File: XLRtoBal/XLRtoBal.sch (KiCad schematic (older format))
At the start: 60 parts, among them J1 XLR4BODYPIN, J10 SMAPCB, J11 SMAPCB, J12 Conn_01x02, J2 Conn_01x04, J3 Conn_01x04, J4 XLR4BODYPIN, J5 Conn_01x04, J6 Conn_01x01, J7 Conn_01x01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

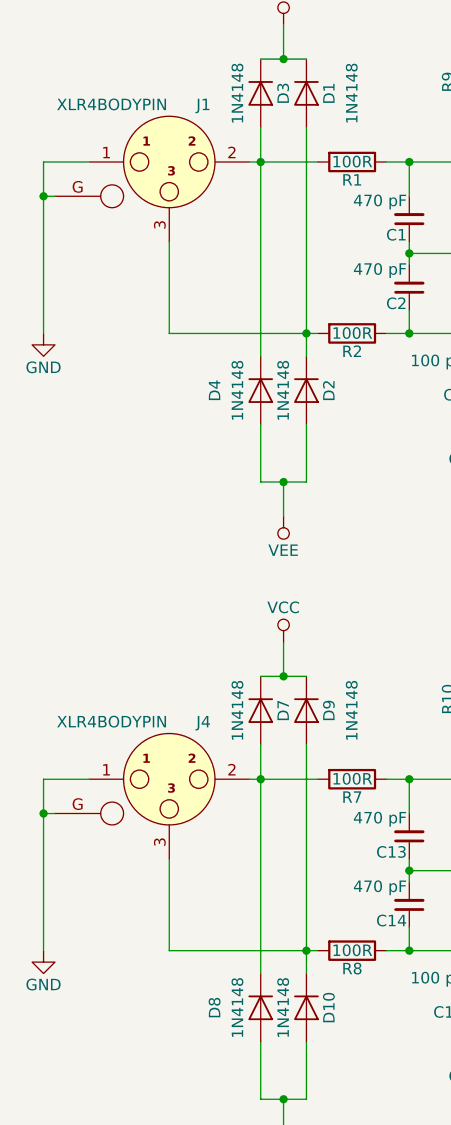
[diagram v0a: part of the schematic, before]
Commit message: Fixed some silkscreening
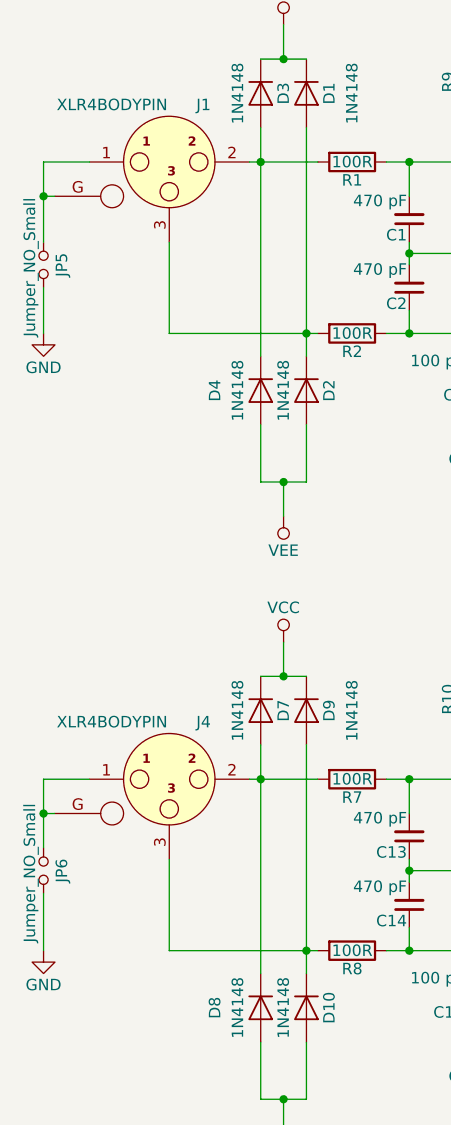
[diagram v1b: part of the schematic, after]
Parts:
- added JP5, JP6: Jumper_NO_Small, Pin_Headers:Pin_Header_Straight_1x02_Pitch2.54mm, symbol Jumper_NO_Small
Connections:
- net GND: now also JP5.2, JP6.2; no longer J1.1, J1.G, J4.1, J4.G
- new net: J1.1, J1.G, JP5.1
- new net: J4.1, J4.G, JP6.1
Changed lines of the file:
@@
 $EndDescr
 $Comp
-L GND #PWR01
+L GND #PWR1
 U 1 1 5F3D3B65
 P 1800 2600
-F 0 "#PWR01" H 1800 2350 50  0001 C CNN
+F 0 "#PWR1" H 1800 2350 50  0001 C CNN
 F 1 "GND" H 1800 2450 50  0000 C CNN
 F 2 "" H 1800 2600 50  0001 C CNN
@@
 $EndComp
 $Comp
-L GND #PWR02
+L GND #PWR7
 U 1 1 5F3D3E2D
 P 3650 3000
-F 0 "#PWR02" H 3650 2750 50  0001 C CNN
+F 0 "#PWR7" H 3650 2750 50  0001 C CNN
 F 1 "GND" H 3650 2850 50  0000 C CNN
 F 2 "" H 3650 3000 50  0001 C CNN
@@
 $EndComp
 $Comp
-L VEE #PWR03
+L VEE #PWR11
 U 1 1 5F3D40DD
 P 4050 2700
-F 0 "#PWR03" H 4050 2550 50  0001 C CNN
+F 0 "#PWR11" H 4050 2550 50  0001 C CNN
 F 1 "VEE" H 4050 2850 50  0000 C CNN
 F 2 "" H 4050 2700 50  0001 C CNN
@@
 $EndComp
 $Comp
-L VCC #PWR04
+L VCC #PWR15
 U 1 1 5F3D4122
 P 5300 1450
-F 0 "#PWR04" H 5300 1300 50  0001 C CNN
+F 0 "#PWR15" H 5300 1300 50  0001 C CNN
 F 1 "VCC" H 5300 1600 50  0000 C CNN
 F 2 "" H 5300 1450 50  0001 C CNN
@@
 $EndComp
 $Comp
-L GND #PWR05
+L GND #PWR13
 U 1 1 5F3D428D
 P 4250 3000
-F 0 "#PWR05" H 4250 2750 50  0001 C CNN
+F 0 "#PWR13" H 4250 2750 50  0001 C CNN
 F 1 "GND" H 4250 2850 50  0000 C CNN
 F 2 "" H 4250 3000 50  0001 C CNN
@@
 $EndComp
 $Comp
-L GND #PWR06
+L GND #PWR17
 U 1 1 5F3D4412
 P 5450 1750
-F 0 "#PWR06" H 5450 1500 50  0001 C CNN
+F 0 "#PWR17" H 5450 1500 50  0001 C CNN
 F 1 "GND" H 5450 1600 50  0000 C CNN
 F 2 "" H 5450 1750 50  0001 C CNN
@@
 $EndComp
 $Comp
-L GND #PWR07
+L GND #PWR9
 U 1 1 5F3D44EC
 P 3950 1950
-F 0 "#PWR07" H 3950 1700 50  0001 C CNN
+F 0 "#PWR9" H 3950 1700 50  0001 C CNN
 F 1 "GND" H 3950 1800 50  0000 C CNN
 F 2 "" H 3950 1950 50  0001 C CNN
@@
 $EndComp
 $Comp
-L VCC #PWR08
+L VCC #PWR3
 U 1 1 5F3D4787
 P 2850 1250
-F 0 "#PWR08" H 2850 1100 50  0001 C CNN
+F 0 "#PWR3" H 2850 1100 50  0001 C CNN
 F 1 "VCC" H 2850 1400 50  0000 C CNN
 F 2 "" H 2850 1250 50  0001 C CNN
@@
 $EndComp
 $Comp
-L VEE #PWR09
+L VEE #PWR4
 U 1 1 5F3D4918
 P 2850 3400
-F 0 "#PWR09" H 2850 3250 50  0001 C CNN
+F 0 "#PWR4" H 2850 3250 50  0001 C CNN
 F 1 "VEE" H 2850 3550 50  0000 C CNN
 F 2 "" H 2850 3400 50  0001 C CNN
@@
 $EndComp
 $Comp
-L GND #PWR010
+L GND #PWR19
 U 1 1 5F3D4B80
 P 6000 2500
-F 0 "#PWR010" H 6000 2250 50  0001 C CNN
+F 0 "#PWR19" H 6000 2250 50  0001 C CNN
 F 1 "GND" H 6000 2350 50  0000 C CNN
 F 2 "" H 6000 2500 50  0001 C CNN
@@
 $EndComp
 $Comp
-L GND #PWR011
+L GND #PWR28
 U 1 1 5F3D5397
 P 8950 2600
-F 0 "#PWR011" H 8950 2350 50  0001 C CNN
+F 0 "#PWR28" H 8950 2350 50  0001 C CNN
 F 1 "GND" H 8950 2450 50  0000 C CNN
 F 2 "" H 8950 2600 50  0001 C CNN
@@
 $EndComp
 $Comp
-L VCC #PWR012
+L VCC #PWR32
 U 1 1 5F3D57A3
 P 10000 1950
-F 0 "#PWR012" H 10000 1800 50  0001 C CNN
+F 0 "#PWR32" H 10000 1800 50  0001 C CNN
 F 1 "VCC" H 10000 2100 50  0000 C CNN
 F 2 "" H 10000 1950 50  0001 C CNN
@@
 $EndComp
 $Comp
-L GND #PWR013
+L GND #PWR25
 U 1 1 5F3D5C25
 P 8500 1250
-F 0 "#PWR013" H 8500 1000 50  0001 C CNN
+F 0 "#PWR25" H 8500 1000 50  0001 C CNN
 F 1 "GND" H 8500 1100 50  0000 C CNN
 F 2 "" H 8500 1250 50  0001 C CNN
@@
 $EndComp
 $Comp
-L GND #PWR014
+L GND #PWR33
 U 1 1 5F3D5DB2
 P 10000 2900
-F 0 "#PWR014" H 10000 2650 50  0001 C CNN
+F 0 "#PWR33" H 10000 2650 50  0001 C CNN
 F 1 "GND" H 10000 2750 50  0000 C CNN
 F 2 "" H 10000 2900 50  0001 C CNN
@@
 $EndComp
 $Comp
-L VEE #PWR015
+L VEE #PWR30
 U 1 1 5F3D67F6
 P 9500 3200
-F 0 "#PWR015" H 9500 3050 50  0001 C CNN
+F 0 "#PWR30" H 9500 3050 50  0001 C CNN
 F 1 "VEE" H 9500 3350 50  0000 C CNN
 F 2 "" H 9500 3200 50  0001 C CNN
@@
 $EndComp
 $Comp
-L GND #PWR016
+L GND #PWR35
 U 1 1 5F3D82E9
 P 10500 2900
-F 0 "#PWR016" H 10500 2650 50  0001 C CNN
+F 0 "#PWR35" H 10500 2650 50  0001 C CNN
 F 1 "GND" H 10500 2750 50  0000 C CNN
 F 2 "" H 10500 2900 50  0001 C CNN
@@
 $EndComp
 $Comp
-L GND #PWR017
+L GND #PWR27
 U 1 1 5F3D8979
 P 8750 2300
-F 0 "#PWR017" H 8750 2050 50  0001 C CNN
+F 0 "#PWR27" H 8750 2050 50  0001 C CNN
 F 1 "GND" H 8750 2150 50  0000 C CNN
 F 2 "" H 8750 2300 50  0001 C CNN
@@
 $EndComp
 $Comp
-L GND #PWR018
+L GND #PWR24
 U 1 1 5F3D8B1C
 P 8400 2650
-F 0 "#PWR018" H 8400 2400 50  0001 C CNN
+F 0 "#PWR24" H 8400 2400 50  0001 C CNN
 F 1 "GND" H 8400 2500 50  0000 C CNN
 F 2 "" H 8400 2650 50  0001 C CNN
@@
 $EndComp
 $Comp
-L GND #PWR019
+L GND #PWR29
 U 1 1 5F3DA1A1
 P 9500 1200
-F 0 "#PWR019" H 9500 950 50  0001 C CNN
+F 0 "#PWR29" H 9500 950 50  0001 C CNN
 F 1 "GND" H 9500 1050 50  0000 C CNN
 F 2 "" H 9500 1200 50  0001 C CNN
@@
 $EndComp
 $Comp
-L GND #PWR020
+L GND #PWR31
 U 1 1 5F3DA52E
 P 9700 3600
-F 0 "#PWR020" H 9700 3350 50  0001 C CNN
+F 0 "#PWR31" H 9700 3350 50  0001 C CNN
 F 1 "GND" H 9700 3450 50  0000 C CNN
 F 2 "" H 9700 3600 50  0001 C CNN
@@
 $EndComp
 $Comp
-L GND #PWR021
+L GND #PWR2
 U 1 1 5F3DAB4A
 P 1800 5300
-F 0 "#PWR021" H 1800 5050 50  0001 C CNN
+F 0 "#PWR2" H 1800 5050 50  0001 C CNN
 F 1 "GND" H 1800 5150 50  0000 C CNN
 F 2 "" H 1800 5300 50  0001 C CNN
@@
 $EndComp
 $Comp
-L GND #PWR022
+L GND #PWR8
 U 1 1 5F3DAB6E
 P 3650 5700
-F 0 "#PWR022" H 3650 5450 50  0001 C CNN
+F 0 "#PWR8" H 3650 5450 50  0001 C CNN
 F 1 "GND" H 3650 5550 50  0000 C CNN
 F 2 "" H 3650 5700 50  0001 C CNN
@@
 $EndComp
 $Comp
-L VEE #PWR023
+L VEE #PWR12
 U 1 1 5F3DAB7A
 P 4050 5400
-F 0 "#PWR023" H 4050 5250 50  0001 C CNN
+F 0 "#PWR12" H 4050 5250 50  0001 C CNN
 F 1 "VEE" H 4050 5550 50  0000 C CNN
 F 2 "" H 4050 5400 50  0001 C CNN
@@
 $EndComp
 $Comp
-L VCC #PWR024
+L VCC #PWR16
 U 1 1 5F3DAB80
 P 5300 4150
-F 0 "#PWR024" H 5300 4000 50  0001 C CNN
+F 0 "#PWR16" H 5300 4000 50  0001 C CNN
 F 1 "VCC" H 5300 4300 50  0000 C CNN
 F 2 "" H 5300 4150 50  0001 C CNN
@@
 $EndComp
 $Comp
-L GND #PWR025
+L GND #PWR14
 U 1 1 5F3DAB8C
 P 4250 5700
-F 0 "#PWR025" H 4250 5450 50  0001 C CNN
+F 0 "#PWR14" H 4250 5450 50  0001 C CNN
 F 1 "GND" H 4250 5550 50  0000 C CNN
 F 2 "" H 4250 5700 50  0001 C CNN
@@
 $EndComp
 $Comp
-L GND #PWR026
+L GND #PWR18
 U 1 1 5F3DAB98
 P 5450 4450
-F 0 "#PWR026" H 5450 4200 50  0001 C CNN
+F 0 "#PWR18" H 5450 4200 50  0001 C CNN
 F 1 "GND" H 5450 4300 50  0000 C CNN
 F 2 "" H 5450 4450 50  0001 C CNN
@@
 $EndComp
 $Comp
-L GND #PWR027
+L GND #PWR10
 U 1 1 5F3DAB9E
 P 3950 4650
-F 0 "#PWR027" H 3950 4400 50  0001 C CNN
+F 0 "#PWR10" H 3950 4400 50  0001 C CNN
 F 1 "GND" H 3950 4500 50  0000 C CNN
 F 2 "" H 3950 4650 50  0001 C CNN
@@
 $EndComp
 $Comp
-L VCC #PWR028
+L VCC #PWR5
 U 1 1 5F3DABB0
 P 2850 3950
-F 0 "#PWR028" H 2850 3800 50  0001 C CNN
+F 0 "#PWR5" H 2850 3800 50  0001 C CNN
 F 1 "VCC" H 2850 4100 50  0000 C CNN
 F 2 "" H 2850 3950 50  0001 C CNN
@@
 $EndComp
 $Comp
-L VEE #PWR029
+L VEE #PWR6
 U 1 1 5F3DABC2
 P 2850 6100
-F 0 "#PWR029" H 2850 5950 50  0001 C CNN
+F 0 "#PWR6" H 2850 5950 50  0001 C CNN
 F 1 "VEE" H 2850 6250 50  0000 C CNN
 F 2 "" H 2850 6100 50  0001 C CNN
@@
 $EndComp
 $Comp
-L GND #PWR030
+L GND #PWR20
 U 1 1 5F3DABD4
 P 6000 5200
-F 0 "#PWR030" H 6000 4950 50  0001 C CNN
+F 0 "#PWR20" H 6000 4950 50  0001 C CNN
 F 1 "GND" H 6000 5050 50  0000 C CNN
 F 2 "" H 6000 5200 50  0001 C CNN
@@
 $EndComp
 $Comp
-L GND #PWR031
+L GND #PWR22
 U 1 1 5F3DC248
 P 6550 4600
-F 0 "#PWR031" H 6550 4350 50  0001 C CNN
+F 0 "#PWR22" H 6550 4350 50  0001 C CNN
 F 1 "GND" H 6550 4450 50  0000 C CNN
 F 2 "" H 6550 4600 50  0001 C CNN
@@
 $EndComp
 $Comp
-L GND #PWR032
+L GND #PWR21
 U 1 1 5F3DC61A
 P 6550 1950
-F 0 "#PWR032" H 6550 1700 50  0001 C CNN
+F 0 "#PWR21" H 6550 1700 50  0001 C CNN
 F 1 "GND" H 6550 1800 50  0000 C CNN
 F 2 "" H 6550 1950 50  0001 C CNN
@@
 $EndComp
 $Comp
-L GND #PWR033
+L GND #PWR23
 U 1 1 5F4033A3
 P 7650 5200
-F 0 "#PWR033" H 7650 4950 50  0001 C CNN
+F 0 "#PWR23" H 7650 4950 50  0001 C CNN
 F 1 "GND" H 7650 5050 50  0000 C CNN
 F 2 "" H 7650 5200 50  0001 C CNN
@@
 $EndComp
 $Comp
-L GND #PWR034
+L GND #PWR26
 U 1 1 5F403644
 P 8600 5250
-F 0 "#PWR034" H 8600 5000 50  0001 C CNN
+F 0 "#PWR26" H 8600 5000 50  0001 C CNN
 F 1 "GND" H 8600 5100 50  0000 C CNN
 F 2 "" H 8600 5250 50  0001 C CNN
@@
 $EndComp
 $Comp
-L GND #PWR035
+L GND #PWR34
 U 1 1 5F85D4C9
 P 10350 4750
-F 0 "#PWR035" H 10350 4500 50  0001 C CNN
+F 0 "#PWR34" H 10350 4500 50  0001 C CNN
 F 1 "GND" H 10350 4600 50  0000 C CNN
 F 2 "" H 10350 4750 50  0001 C CNN
@@
 $EndComp
 Wire Wire Line
-	1800 1850 1800 2600
-Wire Wire Line
 	1800 1850 2000 1850
 Wire Wire Line
@@
 	9500 3600 9700 3600
 Wire Wire Line
-	1800 4550 1800 5300
-Wire Wire Line
 	1800 4550 2000 4550
 Wire Wire Line
@@
 Wire Wire Line
 	8100 1100 8050 1100
+$Comp
+L Jumper_NO_Small JP6
+U 1 1 61461564
+P 1800 4950
+F 0 "JP6" H 1800 5030 50  0000 C CNN
+F 1 "Jumper_NO_Small" H 1810 4890 50  0000 C CNN
+F 2 "Pin_Headers:Pin_Header_Straight_1x02_Pitch2.54mm" H 1800 4950 50  0001 C CNN
+F 3 "" H 1800 4950 50  0001 C CNN
+	1    1800 4950
+	0    1    1    0
+$EndComp
+Wire Wire Line
+	1800 4550 1800 4850
+Wire Wire Line
+	1800 5050 1800 5300
+$Comp
+L Jumper_NO_Small JP5
+U 1 1 61461A8E
+P 1800 2300
+F 0 "JP5" H 1800 2380 50  0000 C CNN
+F 1 "Jumper_NO_Small" H 1810 2240 50  0000 C CNN
+F 2 "Pin_Headers:Pin_Header_Straight_1x02_Pitch2.54mm" H 1800 2300 50  0001 C CNN
+F 3 "" H 1800 2300 50  0001 C CNN
+	1    1800 2300
+	0    1    1    0
+$EndComp
+Wire Wire Line
+	1800 1850 1800 2200
+Wire Wire Line
+	1800 2400 1800 2600
 $EndSCHEMATC
